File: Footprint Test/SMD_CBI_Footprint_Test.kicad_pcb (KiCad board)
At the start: 2 copper layers, 21.3 x 33 mm, 20 parts, among them J1 Conn_01x04

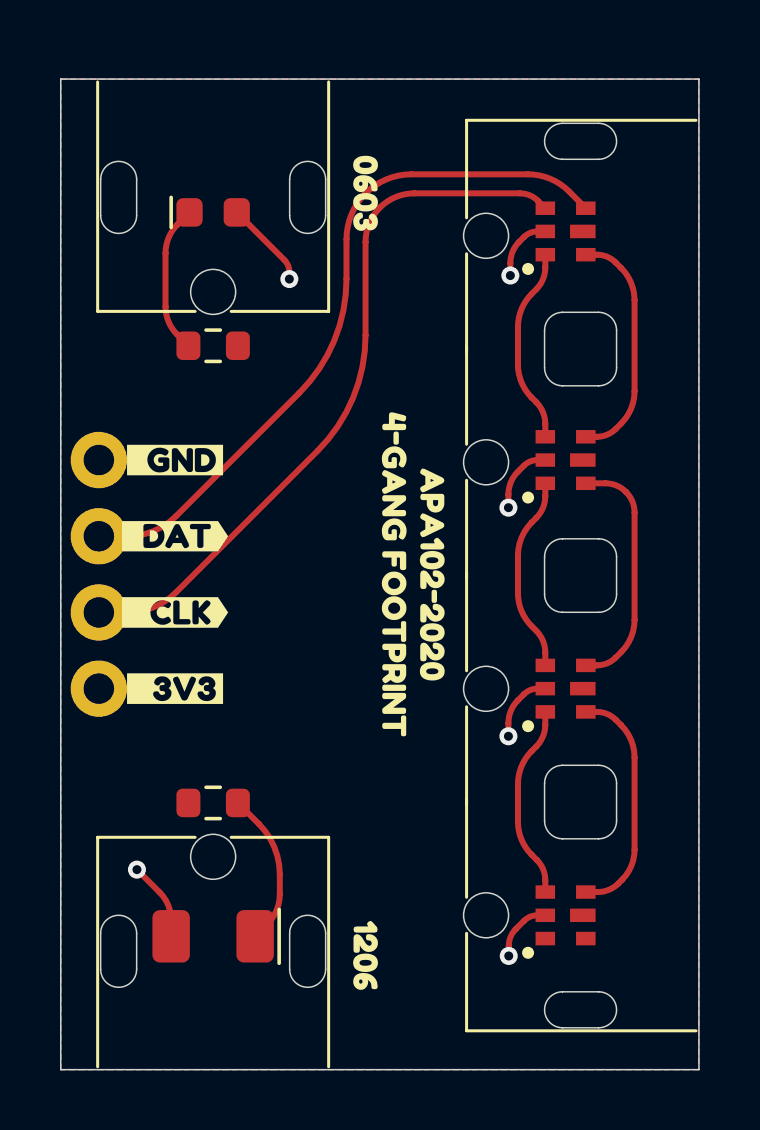
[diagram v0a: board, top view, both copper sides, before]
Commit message: Add courtyard to footprints. Create external KiCad library.
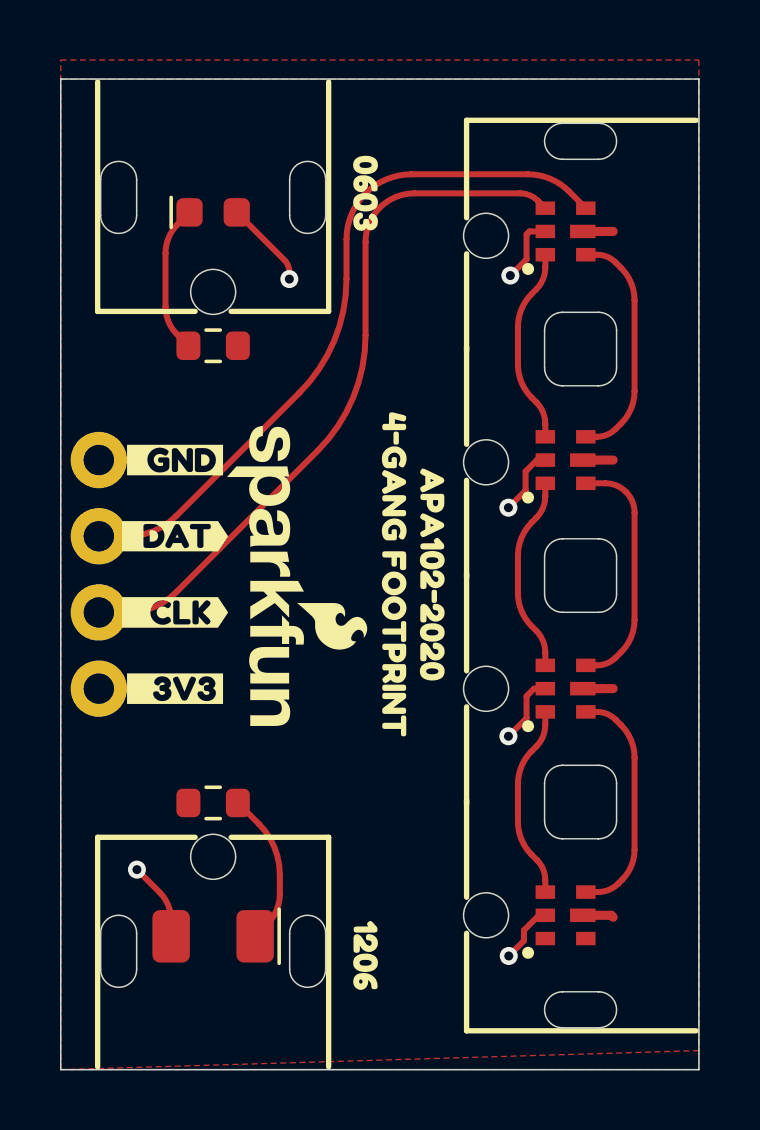
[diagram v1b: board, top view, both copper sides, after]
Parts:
- added G***: LOGO, SparkFun-Aesthetic:SparkFun_Logo_10mm, F.Cu at (99.1, 67.3)
- D2: footprint SparkFun-LED:LED_0603_1608Metric -> SparkFun SMD LED Light Pipe:LED_0603_1608Metric
- D4: footprint SparkFun-LED:LED_1206_3216Metric -> SparkFun SMD LED Light Pipe:LED_1206_3216Metric
- D5, D6, D7, D8: footprint SparkFun-LED:APA-102-2020 -> SparkFun SMD LED Light Pipe:APA-102-2020
- J1: footprint SparkFun-Connector:1x04 -> SparkFun SMD LED Light Pipe:1x04
- R1, R2: footprint SparkFun-Resistor:R_0603_1608Metric -> SparkFun SMD LED Light Pipe:R_0603_1608Metric
- REF** (x2): footprint SparkFun-LED:SMD-CBI -> SparkFun SMD LED Light Pipe:SMD-CBI-5mm
- REF**: footprint SparkFun-LED:SMD-CBI-4GANG -> SparkFun SMD LED Light Pipe:SMD-CBI-5mm-4Gang
- kibuzzard-668F3CFD: footprint kibuzzard-668F3CFD -> SparkFun SMD LED Light Pipe:kibuzzard-668F3CFD
- kibuzzard-668F3D18: footprint kibuzzard-668F3D18 -> SparkFun SMD LED Light Pipe:kibuzzard-668F3D18
- kibuzzard-668F3D36: footprint kibuzzard-668F3D36 -> SparkFun SMD LED Light Pipe:kibuzzard-668F3D36
- kibuzzard-668F3D4E: footprint kibuzzard-668F3D4E -> SparkFun SMD LED Light Pipe:kibuzzard-668F3D4E
- kibuzzard-668F3D73: footprint kibuzzard-668F3D73 -> SparkFun SMD LED Light Pipe:kibuzzard-668F3D73
- kibuzzard-668F3D84: footprint kibuzzard-668F3D84 -> SparkFun SMD LED Light Pipe:kibuzzard-668F3D84
- kibuzzard-668F3D94: footprint kibuzzard-668F3D94 -> SparkFun SMD LED Light Pipe:kibuzzard-668F3D94
- kibuzzard-668F3DA2: footprint kibuzzard-668F3DA2 -> SparkFun SMD LED Light Pipe:kibuzzard-668F3DA2
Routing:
- net GND: track 0.00 -> 4.08 mm
